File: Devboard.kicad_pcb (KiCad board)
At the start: 2 copper layers, 27 parts, among them J1 0-13 pin, J2 A0-A5, J3 Power, P1 USB_C_Plug_USB2.0, SW1 SW_Push, U1 ATmega328-P, U2 CH340G, U3 L7805, Y1 12MHz, Y2 16MHz

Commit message: Pcb
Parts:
- removed C10, C11, C4, C5: 100nF, Capacitor_THT:C_Disc_D5.0mm_W2.5mm_P5.00mm
- removed C16: 10uF, Capacitor_THT:CP_Radial_D5.0mm_P2.00mm
- R2: value 5v -> 5k
- moved J1 182.0 mm to (209.5, 123.6), turned to 180 degrees
- moved U1 157.6 mm to (203.5, 121.1), turned to 180 degrees
- moved U2 143.0 mm to (202.0, 72.0)
- moved C8 129.9 mm to (184.0, 122.5)
- moved C7 118.8 mm to (189.5, 113.0), turned to -90 degrees
- moved P1 116.0 mm to (192.0, 57.0), turned to 180 degrees
- moved C6 115.3 mm to (197.5, 83.5)
- moved C14 112.0 mm to (189.5, 109.0), turned to 90 degrees
- moved C2 108.9 mm to (185.5, 79.5), turned to 180 degrees
- moved C3 108.8 mm to (182.5, 89.0), turned to -90 degrees
- moved C13 107.5 mm to (189.5, 96.5), turned to -90 degrees
- moved Y2 106.6 mm to (183.5, 115.3), turned to 90 degrees
- moved R1 104.5 mm to (192.6, 67.0), turned to 180 degrees
- moved C1 103.6 mm to (181.0, 72.5)
- moved Y1 101.3 mm to (190.5, 73.0), turned to -90 degrees
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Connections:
- U1 pad 21: Net-(U1-AREF) -> +5V
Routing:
- net GND: track 0.00 -> 248.3 mm
- net +5V: track 0.00 -> 201.3 mm
- net /TX: track 0.00 -> 121.5 mm
- net /RX: track 0.00 -> 105.1 mm
- net /RESET: track 0.00 -> 94.2 mm
- net Net-(U1-XTAL1/PB6): track 0.00 -> 85.9 mm
- net Net-(J1-Pin_10): track 0.00 -> 51.9 mm
- net Net-(J1-Pin_14): track 0.00 -> 46.5 mm
- net Net-(U1-XTAL2/PB7): track 0.00 -> 46.1 mm, vias 0 -> 1
- net +3.3V: track 0.00 -> 45.7 mm, vias 0 -> 1
- net Net-(J1-Pin_11): track 0.00 -> 41.2 mm
- net Net-(J2-Pin_1): track 0.00 -> 40.3 mm
- net Net-(J2-Pin_5): track 0.00 -> 39.9 mm
- net Net-(J2-Pin_4): track 0.00 -> 39.5 mm
- net Net-(J2-Pin_3): track 0.00 -> 39.2 mm
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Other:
- board outline added: 36 x 70.5 mm

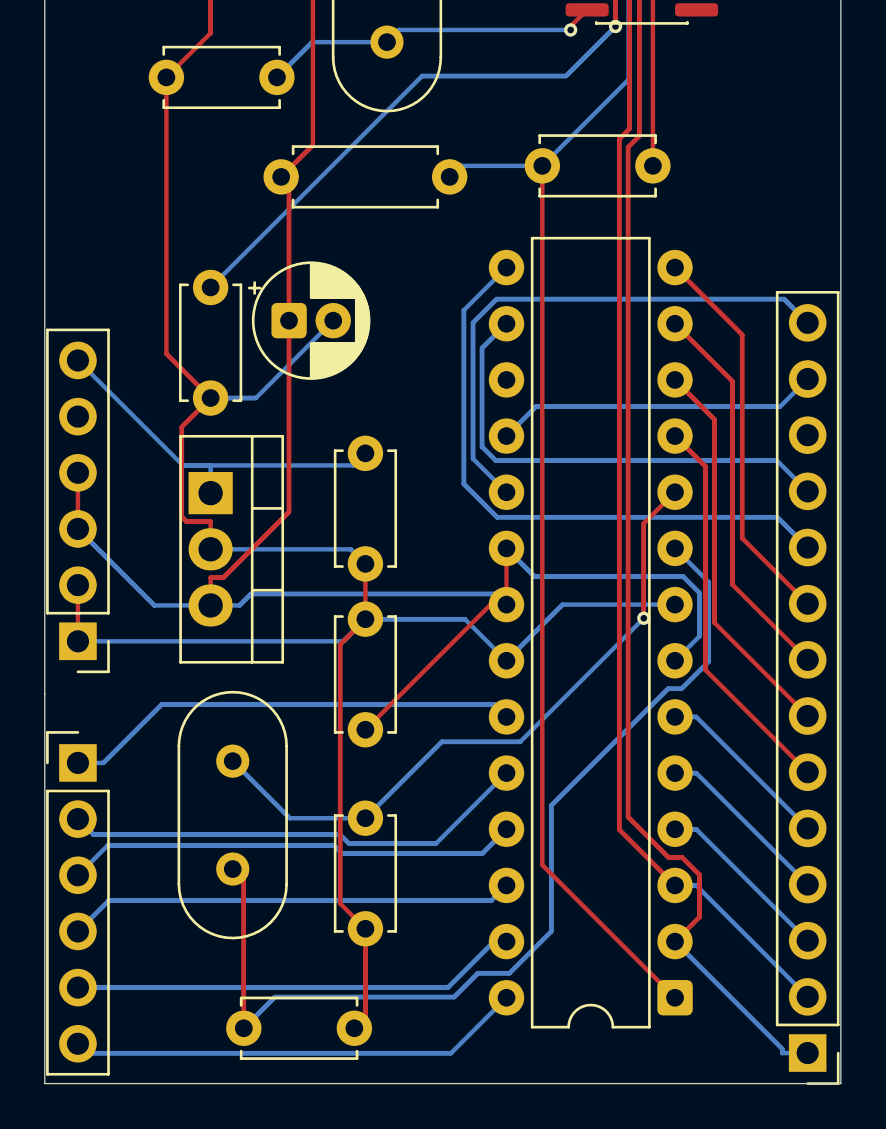
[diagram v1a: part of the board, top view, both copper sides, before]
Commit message: Added pcb lbeling
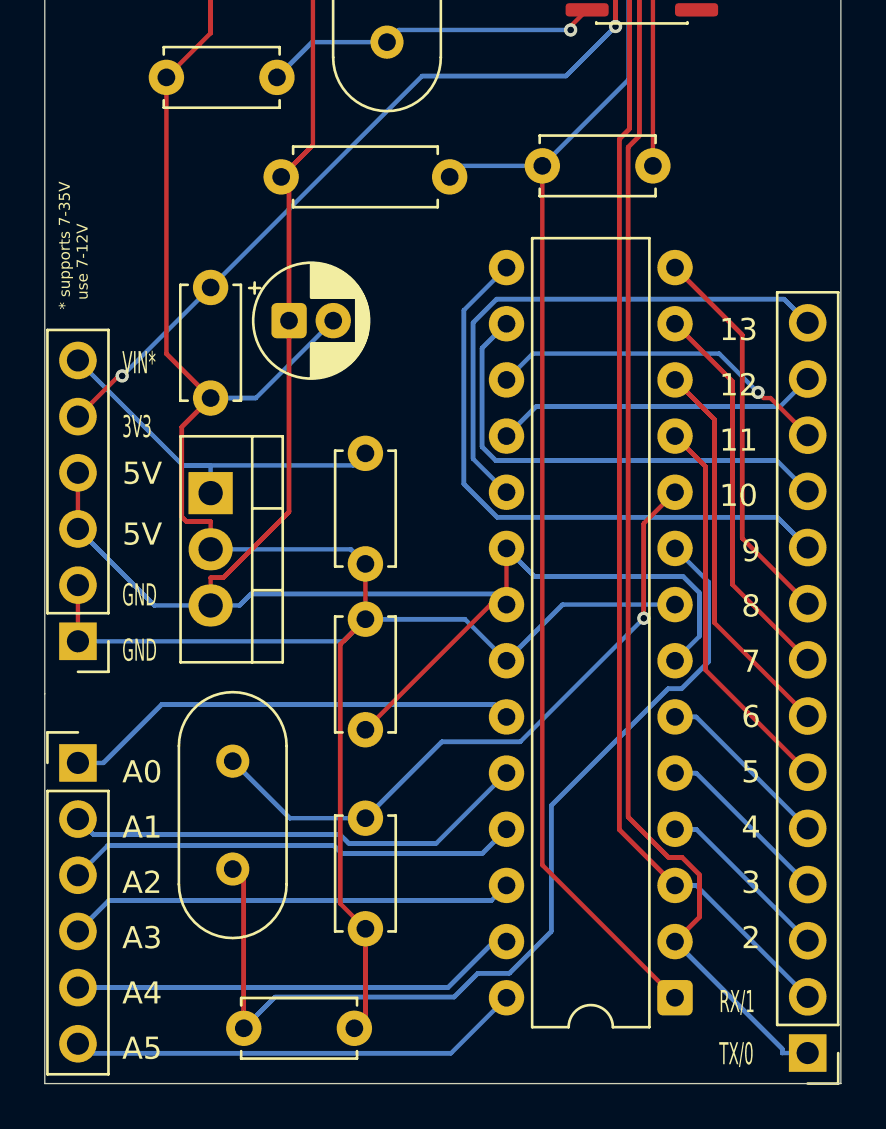
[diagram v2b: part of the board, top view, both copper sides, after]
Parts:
- added G***: LOGO, LOGO, B.Cu at (201.0, 68.5)
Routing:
- net Net-(J1-Pin_12): track 0.00 -> 15.6 mm, vias 0 -> 1
- net +3.3V: track 45.7 -> 54.1 mm, vias 1 -> 2
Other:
- board text added: "* supports 7-35V use 7-12V"
- board text added: "10"
- board text added: "11"
- board text added: "12"
- board text added: "13"
- board text added: "2"
- board text added: "3"
- board text added: "3V3"
- board text added: "4"
- board text added: "5"
- board text added: "5V"
- board text added: "6"
- board text added: "7"
- board text added: "8"
- board text added: "9"
- board text added: "A0"
- board text added: "A1"
- board text added: "A2"
- board text added: "A3"
- board text added: "A4"
- board text added: "A5"
- board text added: "GND"
- board text added: "Made by Apish Rana ;)"
- board text added: "RX/1"
- board text added: "TX/0"
- board text added: "VIN*"

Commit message: pcb
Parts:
- added G***: LOGO, LOGO, B.Cu at (190.5, 117.0)
- added G***: LOGO, LOGO, B.Cu at (202.0, 71.0)
- moved G*** 20.5 mm to (200.5, 89.0)
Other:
- board text added: "67"
- board text added: "art by @lulalang_"
